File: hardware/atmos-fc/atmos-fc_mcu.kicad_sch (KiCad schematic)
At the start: 33 parts, among them Q1 BC817, SW1 SW_Push, U3 STM32G473CEU6, Y1 8MHz

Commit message: Add GYRO_1_EXTI Pin
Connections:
- net IMU_INT: now reaches U3.32 (PA10)
- net BUZZER_CTRL renamed BUZZER_EN
- net BUZZER_CTRL_B renamed BUZZER_EN_B
- no-connect marks 5 -> 4
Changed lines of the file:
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@@
 	)
 	(bus_alias "IMU_COM."
-		(members "IMU_SPI_~{CS}" "IMU_SPI_SCK" "IMU_SPI_MISO" "IMU_SPI_MOSI")
+		(members "IMU_SPI_~{CS}" "IMU_SPI_SCK" "IMU_SPI_MISO" "IMU_SPI_MOSI" "IMU_INT")
 	)
 	(bus_alias "OSD_COM."
@@
 	)
 	(no_connect
-		(at 219.71 91.44)
-	)
-	(no_connect
 		(at 186.69 83.82)
 	)
@@
 	)
 	(bus_entry
+		(at 64.77 153.67)
+		(size 2.54 2.54)
+		(stroke
+			(width 0)
+			(type default)
+		)
+	)
+	(bus_entry
 		(at 39.37 146.05)
 		(size 2.54 2.54)
@@
 		)
 	)
+	(wire
+		(pts
+			(xy 219.71 91.44) (xy 220.98 91.44)
+		)
+		(stroke
+			(width 0)
+			(type default)
+		)
+	)
 	(bus
 		(pts
@@
 		)
 	)
+	(bus
+		(pts
+			(xy 64.77 151.13) (xy 64.77 153.67)
+		)
+		(stroke
+			(width 0)
+			(type default)
+		)
+	)
 	(wire
 		(pts
@@
 		)
 	)
+	(bus
+		(pts
+			(xy 64.77 153.67) (xy 64.77 156.21)
+		)
+		(stroke
+			(width 0)
+			(type default)
+		)
+	)
 	(wire
 		(pts
@@
 		)
 	)
+	(wire
+		(pts
+			(xy 67.31 156.21) (xy 68.58 156.21)
+		)
+		(stroke
+			(width 0)
+			(type default)
+		)
+	)
 	(bus
 		(pts
@@
 		)
 	)
-	(bus
-		(pts
-			(xy 64.77 151.13) (xy 64.77 153.67)
-		)
-		(stroke
-			(width 0)
-			(type default)
-		)
-	)
 	(wire
 		(pts
@@
 		)
 	)
+	(label "IMU_EXTI"
+		(at 68.58 156.21 0)
+		(fields_autoplaced yes)
+		(effects
+			(font
+				(face "Arial")
+				(size 1.016 1.016)
+			)
+			(justify left bottom)
+		)
+	)
 	(label "LED_BLUE_EN"
 		(at 185.42 96.52 180)
@@
 		)
 	)
-	(label "BUZZER_CTRL_B"
+	(label "BUZZER_EN_B"
 		(at 40.64 64.77 0)
 		(fields_autoplaced yes)
@@
 		)
 	)
-	(label "BUZZER_CTRL"
+	(label "BUZZER_EN"
 		(at 185.42 86.36 180)
 		(fields_autoplaced yes)
@@
 		)
 	)
+	(label "IMU_INT"
+		(at 220.98 91.44 0)
+		(fields_autoplaced yes)
+		(effects
+			(font
+				(face "Arial")
+				(size 1.016 1.016)
+			)
+			(justify left bottom)
+		)
+	)
 	(label "LED1_A"
 		(at 102.87 62.23 0)
@@
 		)
 	)
-	(label "BUZZER_CTRL"
+	(label "BUZZER_EN"
 		(at 31.75 64.77 180)
 		(fields_autoplaced yes)

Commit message: Add soldering pads for ESC
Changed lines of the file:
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@@
 		)
 	)
-	(label "IMU_EXTI"
+	(label "IMU_INT"
 		(at 68.58 156.21 0)
 		(fields_autoplaced yes)

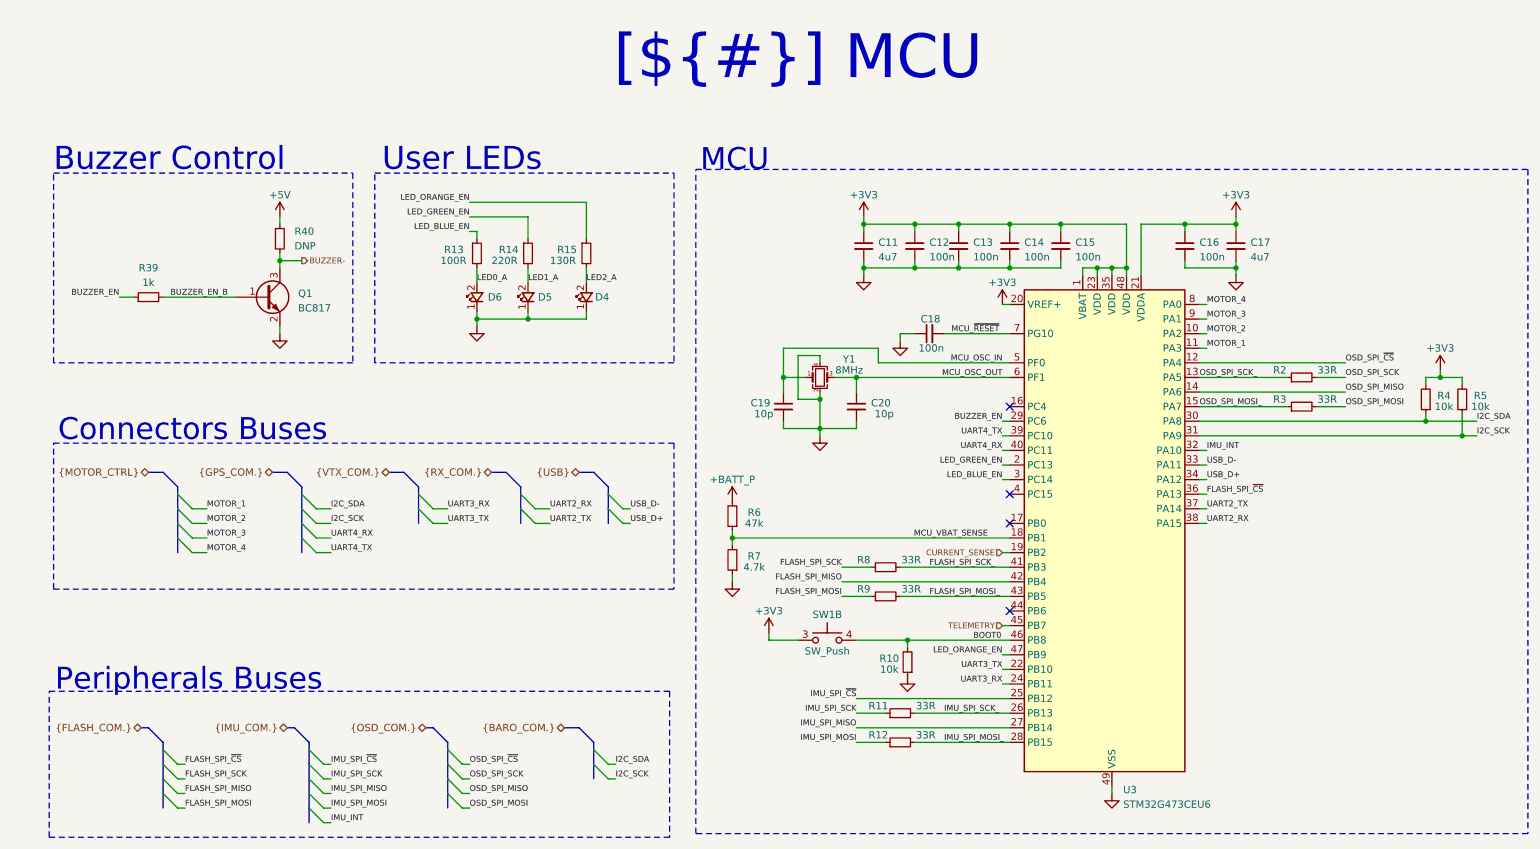
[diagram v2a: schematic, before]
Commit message: Added 100n on ADC inputs and improved layout
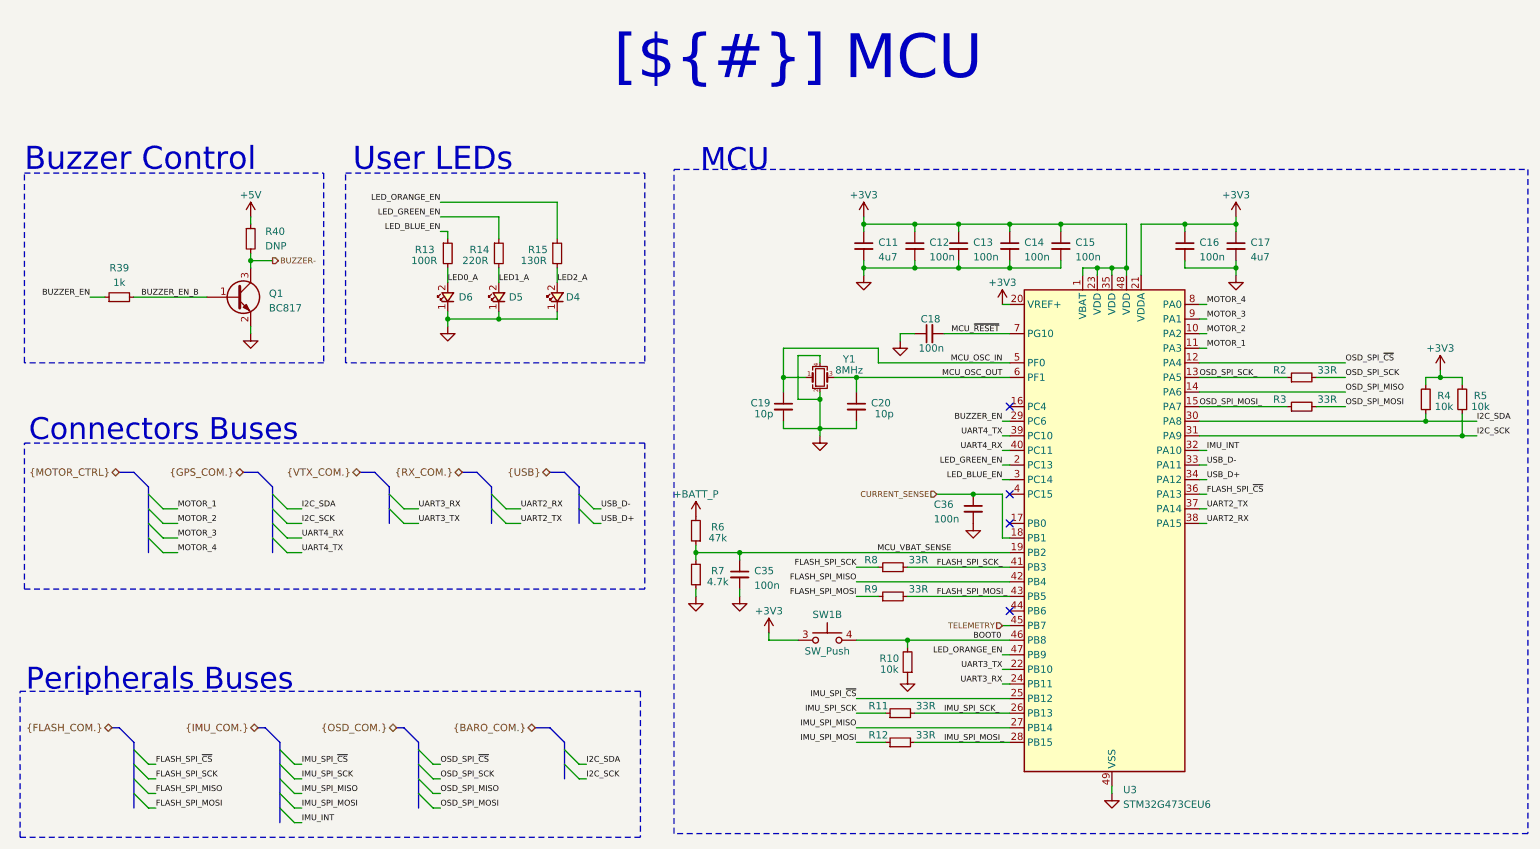
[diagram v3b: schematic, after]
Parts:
- added C35, C36: 100n, Capacitor_SMD:C_0402_1005Metric, symbol Device:C_Small
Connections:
- net CURRENT_SENSE: now also U3.18 (PB1), C36.1; no longer U3.19 (PB2)
- net GND: now also C35.2, C36.2
- net MCU_VBAT_SENSE: now also U3.19 (PB2), C35.1; no longer U3.18 (PB1)
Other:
- moved on the sheet: D4, D5, D6, Q1, R13, R14, R15, R39, R40, R6, R7, R8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
